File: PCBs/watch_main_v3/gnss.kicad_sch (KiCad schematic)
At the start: 8 parts, among them IC401 BGA725L6E6327FTSA1, U401 TESEO-LIV3FL

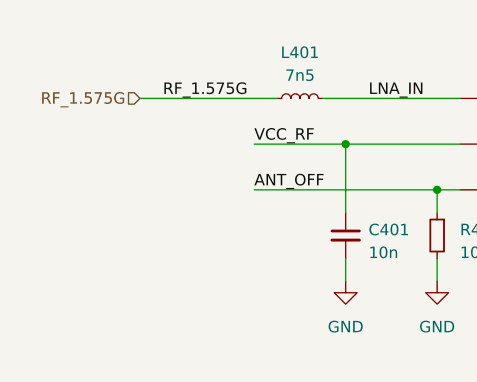
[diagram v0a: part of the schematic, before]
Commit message: watch_main_v3 WiFi/Bluetooth schematic done
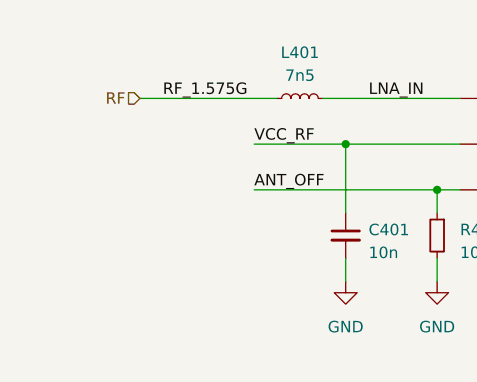
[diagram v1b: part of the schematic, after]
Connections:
- net RF_1.575G renamed RF
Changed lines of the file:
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@@
     )
   )
-  (hierarchical_label "RF_1.575G" (shape input) (at 53.34 81.28 180) (fields_autoplaced)
+  (hierarchical_label "RF" (shape input) (at 53.34 81.28 180) (fields_autoplaced)
     (effects (font (size 1.27 1.27)) (justify right))
   )
